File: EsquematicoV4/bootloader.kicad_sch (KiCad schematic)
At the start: 18 parts, among them J2 USB_B_Micro, Q1 SS8050-G, Q2 SS8050-G, U7 CP2102N-Axx-xQFN28

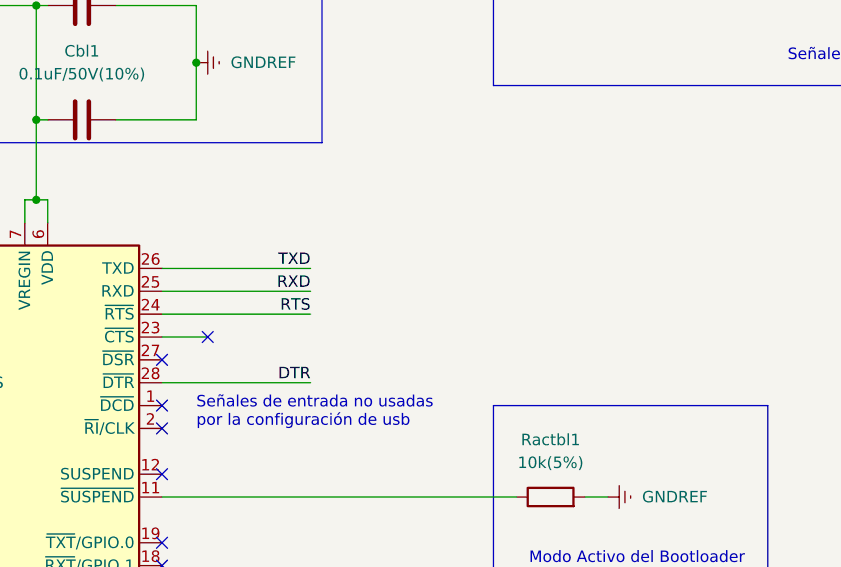
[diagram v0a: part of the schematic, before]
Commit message: Correciones Finales Esquemático - Revisar error con huella del Amplificador de Sonido
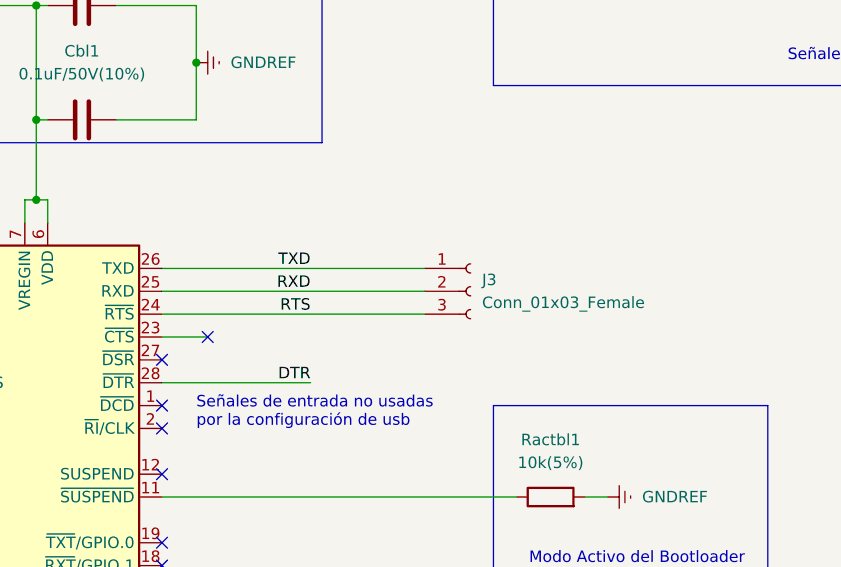
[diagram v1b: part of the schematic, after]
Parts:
- added J3: Conn_01x03_Female, Connector_PinHeader_2.54mm:PinHeader_1x03_P2.54mm_Vertical, symbol Connector:Conn_01x03_Female
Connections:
- net RTS: now also J3.3 (Pin_3)
- net RXD: now also J3.2 (Pin_2)
- net TXD: now also J3.1 (Pin_1)
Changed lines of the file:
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@@
     (stroke (width 0) (type default) (color 0 0 0 0))
   )
-  (wire (pts (xy 157.48 97.79) (xy 173.99 97.79))
+  (wire (pts (xy 157.48 97.79) (xy 186.69 97.79))
     (stroke (width 0) (type default) (color 0 0 0 0))
   )
@@
     (stroke (width 0) (type default) (color 0 0 0 0))
   )
-  (wire (pts (xy 157.48 92.71) (xy 173.99 92.71))
+  (wire (pts (xy 157.48 92.71) (xy 186.69 92.71))
     (stroke (width 0) (type default) (color 0 0 0 0))
   )
@@
     (stroke (width 0) (type default) (color 0 0 0 0))
   )
-  (wire (pts (xy 157.48 95.25) (xy 173.99 95.25))
+  (wire (pts (xy 157.48 95.25) (xy 186.69 95.25))
     (stroke (width 0) (type default) (color 0 0 0 0))
   )
@@
   )
   (text "https://co.mouser.com/ProductDetail/Diodes-Incorporated/BAT760-7?qs=JV7lzlMm3yKDDyO09xoRbQ%3D%3D"
-    (at 121.92 17.78 0)
+    (at 121.92 17.78 180)
     (effects (font (size 1.27 1.27)) (justify right bottom))
   )
@@
     (pin "1")
   )
+  (symbol (lib_id "Connector:Conn_01x03_Female") (at 191.77 95.25 0) (unit 1)
+    (in_bom yes) (on_board yes) (fields_autoplaced)
+    (property "Reference" "J3" (id 0) (at 193.04 93.9799 0)
+      (effects (font (size 1.27 1.27)) (justify left))
+    )
+    (property "Value" "Conn_01x03_Female" (id 1) (at 193.04 96.5199 0)
+      (effects (font (size 1.27 1.27)) (justify left))
+    )
+    (property "Footprint" "Connector_PinHeader_2.54mm:PinHeader_1x03_P2.54mm_Vertical" (id 2) (at 191.77 95.25 0)
+      (effects (font (size 1.27 1.27)) hide)
+    )
+    (property "Datasheet" "~" (id 3) (at 191.77 95.25 0)
+      (effects (font (size 1.27 1.27)) hide)
+    )
+    (pin "1")
+    (pin "2")
+    (pin "3")
+  )
   (symbol (lib_id "SS8050-G:SS8050-G") (at 58.42 168.91 0) (mirror x) (unit 1)
